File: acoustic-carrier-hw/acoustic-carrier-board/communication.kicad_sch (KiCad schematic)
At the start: 46 parts, among them IC1 ECP5-BGA256, J9 HR911130A, U1 KSZ9031RN, Y1 25MHz

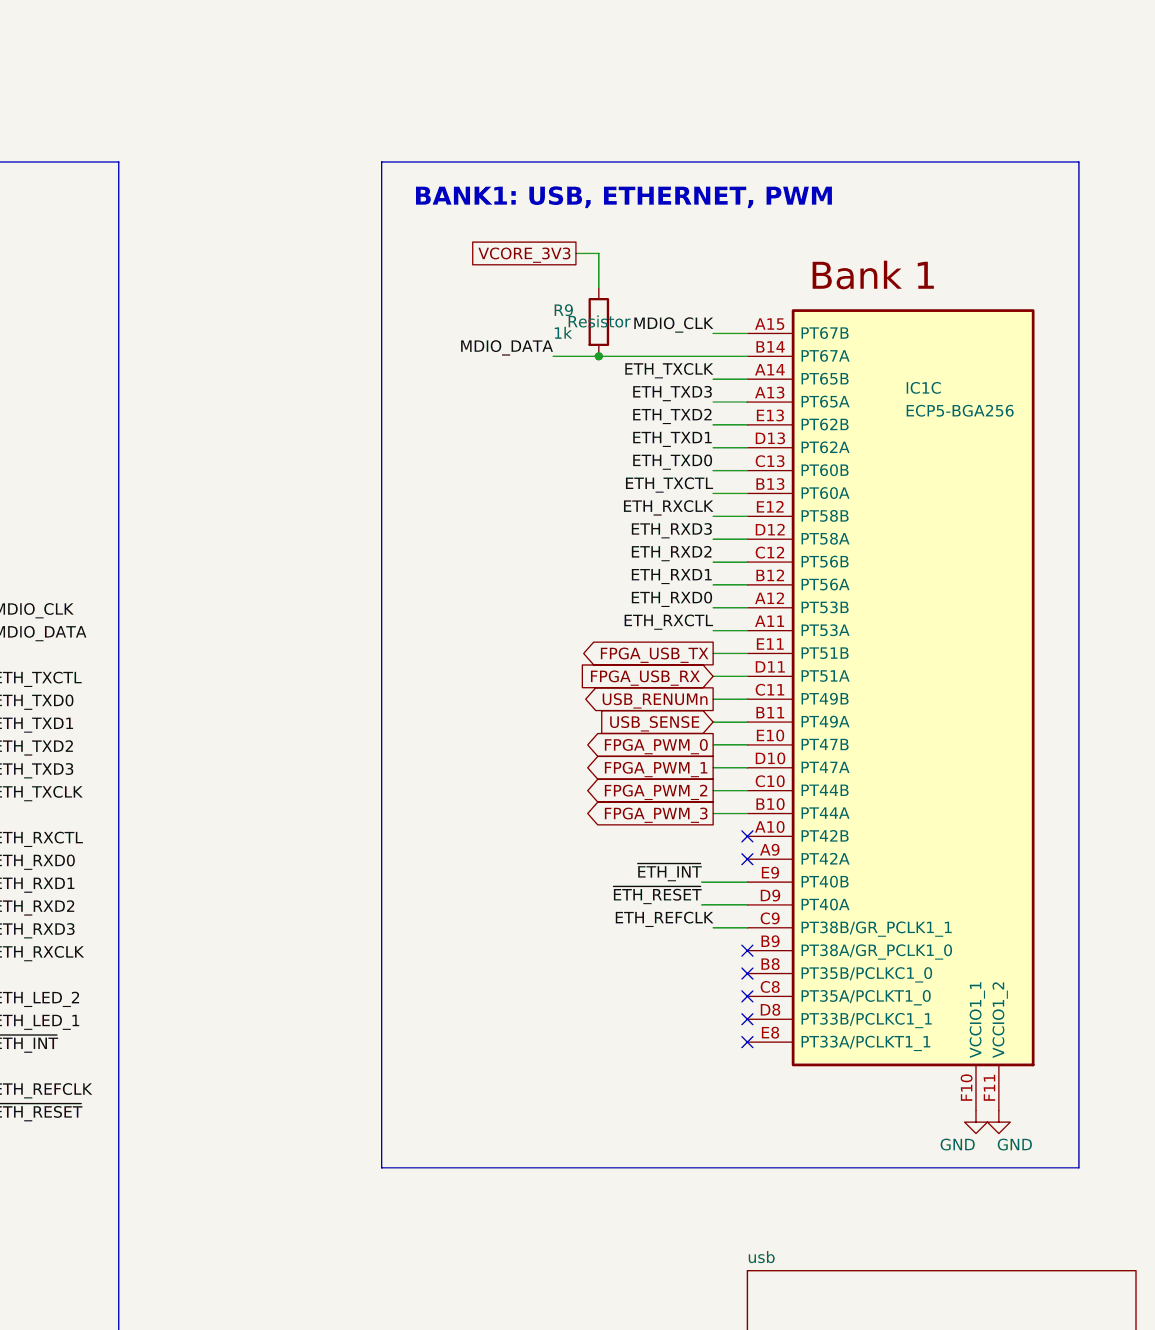
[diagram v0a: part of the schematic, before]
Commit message: [carrier] Fixed minor symbol errors, added minor routing info (next) continue schematic check
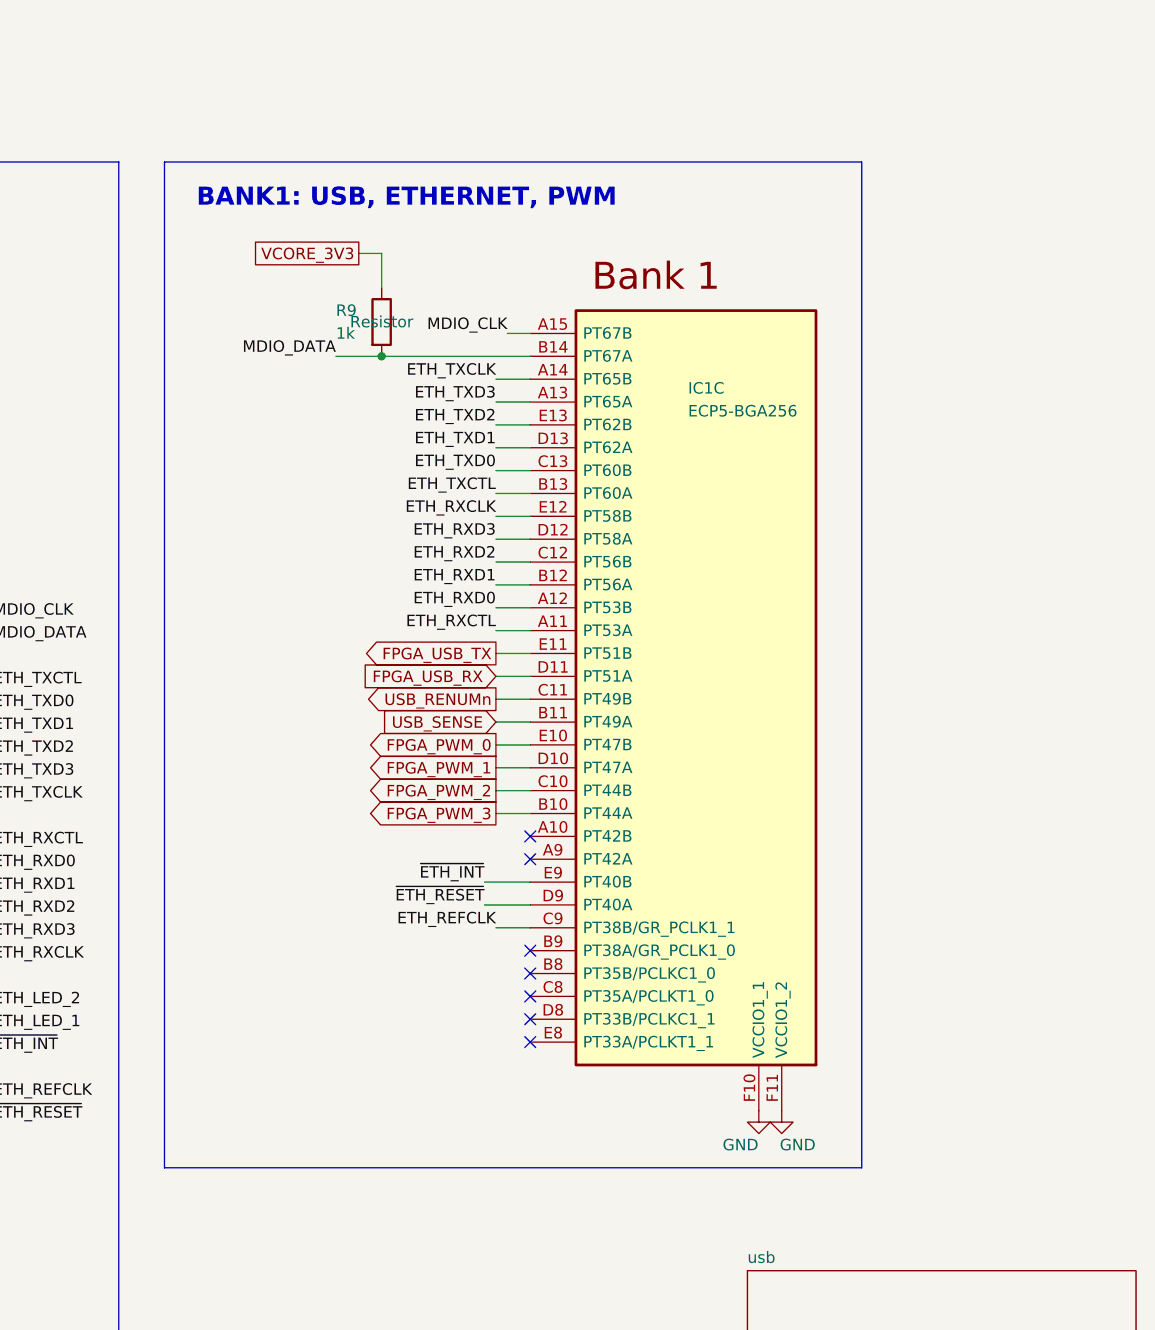
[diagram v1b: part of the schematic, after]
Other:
- moved on the sheet: IC1C, R9

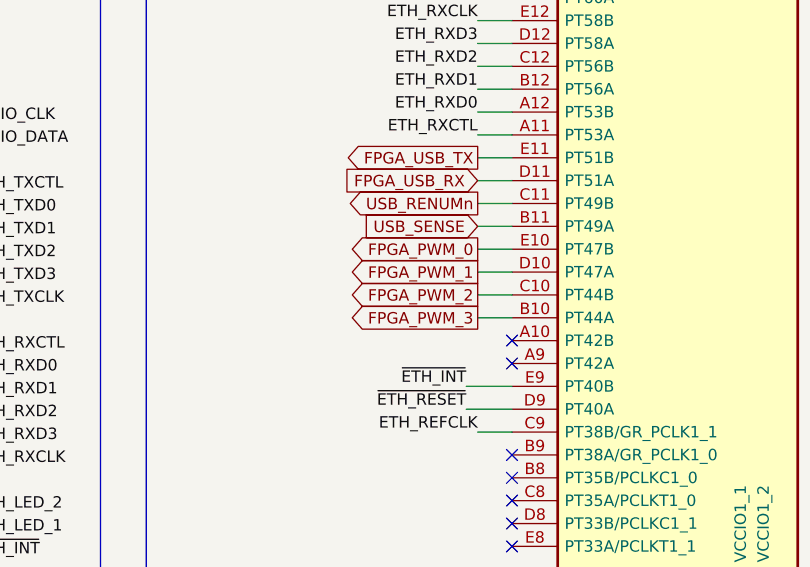
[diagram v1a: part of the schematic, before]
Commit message: [carrier] Review of adc_connections-page done
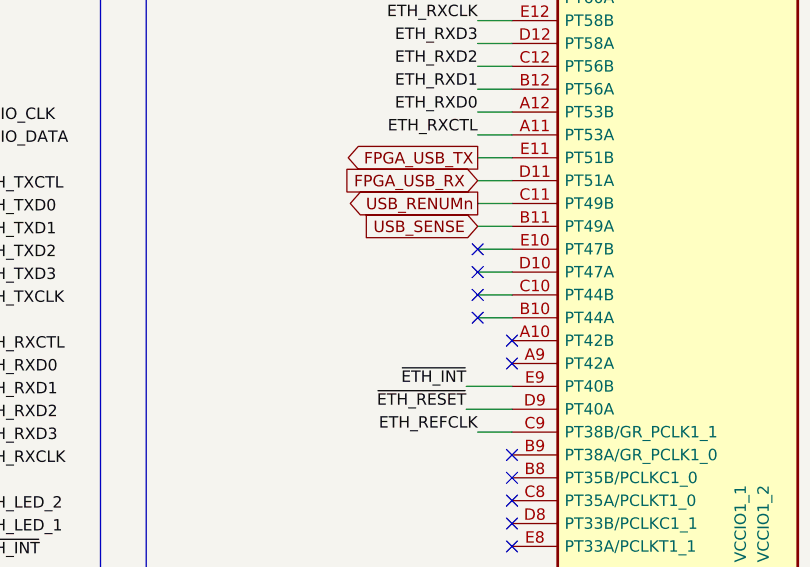
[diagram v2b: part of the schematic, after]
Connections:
- net FPGA_PWM_0: no longer names the net of IC1.E10 (PT47B)
- net FPGA_PWM_1: no longer names the net of IC1.D10 (PT47A)
- net FPGA_PWM_2: no longer names the net of IC1.C10 (PT44B)
- net FPGA_PWM_3: no longer names the net of IC1.B10 (PT44A)
- no-connect marks 8 -> 12
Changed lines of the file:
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@@
+	)
+	(no_connect
+		(at 207.01 85.09)
 	)
 	(no_connect
@@
 		(at 210.82 113.03)
 	)
+	(no_connect
+		(at 207.01 82.55)
+	)
+	(no_connect
+		(at 207.01 87.63)
+	)
+	(no_connect
+		(at 207.01 80.01)
+	)
 	(wire
 		(pts
@@
 			)
 			(justify left bottom)
-		)
-	)
-	(global_label "FPGA_PWM_1"
-		(shape output)
-		(at 207.01 82.55 180)
-		(fields_autoplaced yes)
-		(effects
-			(font
-				(size 1.27 1.27)
-			)
-			(justify right)
-		)
-		(property "Intersheetrefs" "${INTERSHEET_REFS}"
-			(at 191.9901 82.55 0)
-			(effects
-				(font
-					(size 1.27 1.27)
-				)
-				(justify right)
-				(hide yes)
-			)
 		)
 	)
@@
 		)
 	)
-	(global_label "FPGA_PWM_0"
-		(shape output)
-		(at 207.01 80.01 180)
-		(fields_autoplaced yes)
-		(effects
-			(font
-				(size 1.27 1.27)
-			)
-			(justify right)
-		)
-		(property "Intersheetrefs" "${INTERSHEET_REFS}"
-			(at 191.9901 80.01 0)
-			(effects
-				(font
-					(size 1.27 1.27)
-				)
-				(justify right)
-				(hide yes)
-			)
-		)
-	)
 	(global_label "VCORE_3V3"
 		(shape passive)
@@
 		)
 	)
-	(global_label "FPGA_PWM_2"
-		(shape output)
-		(at 207.01 85.09 180)
-		(fields_autoplaced yes)
-		(effects
-			(font
-				(size 1.27 1.27)
-			)
-			(justify right)
-		)
-		(property "Intersheetrefs" "${INTERSHEET_REFS}"
-			(at 191.9901 85.09 0)
-			(effects
-				(font
-					(size 1.27 1.27)
-				)
-				(justify right)
-				(hide yes)
-			)
-		)
-	)
 	(global_label "VCORE_3V3"
 		(shape passive)
@@
 			(effects
 				(font
-					(size 1.27 1.27)
-				)
-				(justify right)
-				(hide yes)
-			)
-		)
-	)
-	(global_label "FPGA_PWM_3"
-		(shape output)
-		(at 207.01 87.63 180)
-		(fields_autoplaced yes)
-		(effects
-			(font
-				(size 1.27 1.27)
-			)
-			(justify right)
-		)
-		(property "Intersheetrefs" "${INTERSHEET_REFS}"
-			(at 191.9901 87.63 0)
-			(effects
-				(font

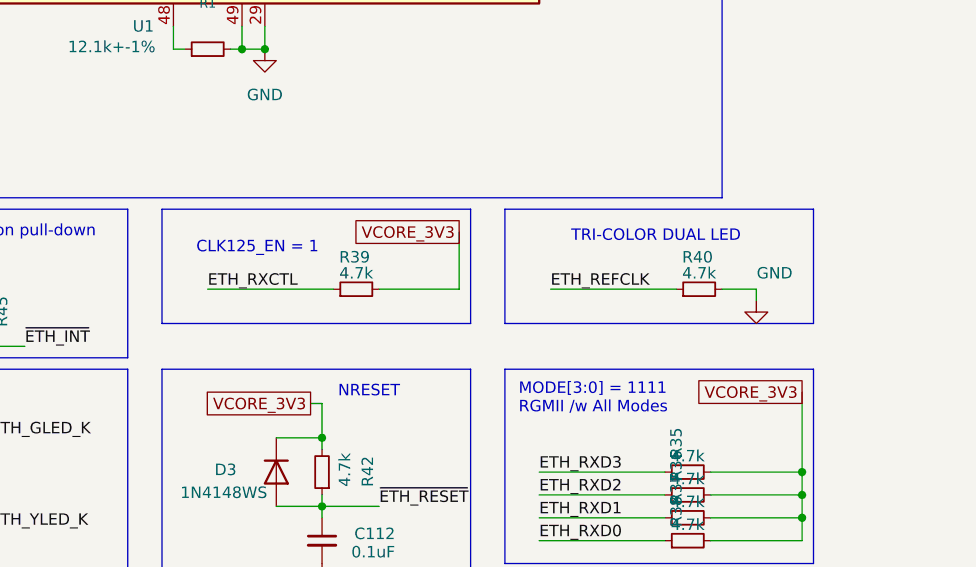
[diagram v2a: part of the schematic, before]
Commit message: [carrier] Finished flash and config check
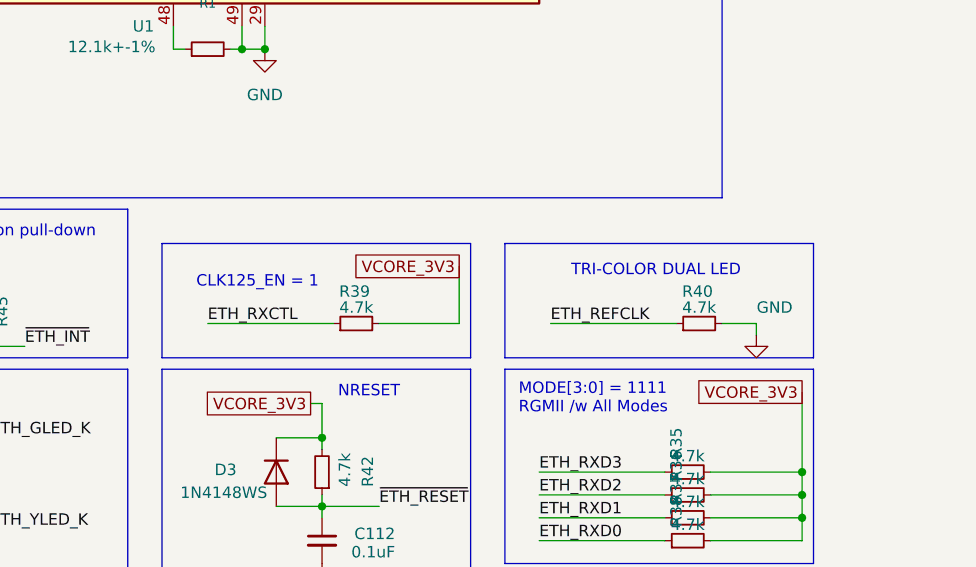
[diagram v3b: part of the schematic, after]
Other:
- moved on the sheet: R39, R40
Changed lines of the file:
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@@
 	(paper "A4")
 	(rectangle
-		(start 140.97 152.4)
-		(end 175.26 165.1)
+		(start 140.97 156.21)
+		(end 175.26 168.91)
 		(stroke
 			(width 0)
@@
 	)
 	(rectangle
-		(start 102.87 152.4)
-		(end 137.16 165.1)
+		(start 102.87 156.21)
+		(end 137.16 168.91)
 		(stroke
 			(width 0)
@@
 	(text "TRI-COLOR DUAL LED"
 		(exclude_from_sim no)
-		(at 148.336 156.21 0)
+		(at 148.336 160.02 0)
 		(effects
 			(font
@@
 	(text "CLK125_EN = 1"
 		(exclude_from_sim no)
-		(at 106.68 157.48 0)
+		(at 106.68 161.29 0)
 		(effects
 			(font
@@
 	(wire
 		(pts
-			(xy 127 161.29) (xy 135.89 161.29)
+			(xy 127 165.1) (xy 135.89 165.1)
 		)
 		(stroke
@@
 	(wire
 		(pts
-			(xy 165.1 161.29) (xy 168.91 161.29)
+			(xy 165.1 165.1) (xy 168.91 165.1)
 		)
 		(stroke
@@
 	(wire
 		(pts
-			(xy 107.95 161.29) (xy 121.92 161.29)
+			(xy 107.95 165.1) (xy 121.92 165.1)
 		)
 		(stroke
@@
 	(wire
 		(pts
-			(xy 135.89 154.94) (xy 135.89 161.29)
+			(xy 135.89 158.75) (xy 135.89 165.1)
 		)
 		(stroke
@@
 	(wire
 		(pts
-			(xy 146.05 161.29) (xy 160.02 161.29)
+			(xy 146.05 165.1) (xy 160.02 165.1)
 		)
 		(stroke
@@
 	(wire
 		(pts
-			(xy 168.91 161.29) (xy 168.91 162.56)
+			(xy 168.91 165.1) (xy 168.91 166.37)
 		)
 		(stroke
@@
 	)
 	(label "ETH_REFCLK"
-		(at 146.05 161.29 0)
+		(at 146.05 165.1 0)
 		(effects
 			(font
@@
 	)
 	(label "ETH_RXCTL"
-		(at 107.95 161.29 0)
+		(at 107.95 165.1 0)
 		(effects
 			(font
@@
 	(global_label "VCORE_3V3"
 		(shape passive)
-		(at 135.89 154.94 180)
+		(at 135.89 158.75 180)
 		(fields_autoplaced yes)
 		(effects
@@
 		)
 		(property "Intersheetrefs" "${INTERSHEET_REFS}"
-			(at 123.4328 154.94 0)
+			(at 123.4328 158.75 0)
 			(effects
 				(font
@@
 	(symbol
 		(lib_id "power:GND")
-		(at 168.91 162.56 0)
+		(at 168.91 166.37 0)
 		(unit 1)
 		(exclude_from_sim no)
@@
 		(dnp no)
 		(property "Reference" "#PWR075"
-			(at 168.91 168.91 0)
+			(at 168.91 172.72 0)
 			(effects
 				(font
@@
 		)
 		(property "Value" "GND"
-			(at 170.942 159.512 0)
+			(at 170.942 163.322 0)
 			(effects
 				(font
@@
 		)
 		(property "Footprint" ""
-			(at 168.91 162.56 0)
+			(at 168.91 166.37 0)
 			(effects
 				(font
@@
 		)
 		(property "Datasheet" ""
-			(at 168.91 162.56 0)
+			(at 168.91 166.37 0)
 			(effects
 				(font
@@
 		)
 		(property "Description" "Power symbol creates a global label with name \"GND\" , ground"
-			(at 168.91 162.56 0)
+			(at 168.91 166.37 0)
 			(effects
 				(font
@@
 	(symbol
 		(lib_id "Device:R_Small")
-		(at 162.56 161.29 90)
+		(at 162.56 165.1 90)
 		(unit 1)
 		(exclude_from_sim no)
@@
 		(dnp no)
 		(property "Reference" "R40"
-			(at 164.084 157.734 90)
+			(at 164.084 161.544 90)
 			(effects
 				(font
@@
 		)
 		(property "Value" "4.7k"
-			(at 162.56 159.512 90)
+			(at 162.56 163.322 90)
 			(effects
 				(font
@@
 		)
 		(property "Footprint" "Resistor_SMD:R_0402_1005Metric"
-			(at 162.56 161.29 0)
+			(at 162.56 165.1 0)
 			(effects
 				(font
@@
 		)
 		(property "Datasheet" "~"
-			(at 162.56 161.29 0)
+			(at 162.56 165.1 0)
 			(effects
 				(font
@@
 		)
 		(property "Description" "Resistor, small symbol"
-			(at 162.56 161.29 0)
+			(at 162.56 165.1 0)
 			(effects
 				(font
@@
 		)
 		(property "LCSC Part Number" ""
-			(at 162.56 161.29 0)
+			(at 162.56 165.1 0)
 			(effects
 				(font
@@
 		)
 		(property "Manufacturing Part Number" ""
-			(at 162.56 161.29 0)
+			(at 162.56 165.1 0)
 			(effects
 				(font
@@
 		)
 		(property "LPN" "0402WGF4701TCE"
-			(at 162.56 161.29 90)
+			(at 162.56 165.1 90)
 			(effects
 				(font
@@
 		)
 		(property "MPN" "C25900"
-			(at 162.56 161.29 90)
+			(at 162.56 165.1 90)
 			(effects
 				(font
@@
 		)
 		(property "Part Number" ""
-			(at 162.56 161.29 90)
+			(at 162.56 165.1 90)
 			(effects
 				(font
@@
 		)
 		(property "SN-DK" ""
-			(at 162.56 161.29 90)
+			(at 162.56 165.1 90)
 			(effects
 				(font
@@
 		)
 		(property "Sim.Pin" ""
-			(at 162.56 161.29 90)
+			(at 162.56 165.1 90)
 			(effects
 				(font
@@
 		)
 		(property "LCSC Part" ""
-			(at 162.56 161.29 90)
+			(at 162.56 165.1 90)
 			(effects
 				(font
@@
 	(symbol
 		(lib_id "Device:R_Small")
-		(at 124.46 161.29 90)
+		(at 124.46 165.1 90)
 		(unit 1)
 		(exclude_from_sim no)
@@
 		(dnp no)
 		(property "Reference" "R39"
-			(at 125.984 157.734 90)
+			(at 125.984 161.544 90)
 			(effects
 				(font
@@
 		)
 		(property "Value" "4.7k"
-			(at 124.46 159.512 90)
+			(at 124.46 163.322 90)
 			(effects
 				(font
@@
 		)
 		(property "Footprint" "Resistor_SMD:R_0402_1005Metric"
-			(at 124.46 161.29 0)
+			(at 124.46 165.1 0)
 			(effects
 				(font
@@
 		)
 		(property "Datasheet" "~"
-			(at 124.46 161.29 0)
+			(at 124.46 165.1 0)
 			(effects
 				(font
@@
 		)
 		(property "Description" "Resistor, small symbol"
-			(at 124.46 161.29 0)
+			(at 124.46 165.1 0)
 			(effects
 				(font
@@
 		)
 		(property "LCSC Part Number" ""
-			(at 124.46 161.29 0)
+			(at 124.46 165.1 0)
 			(effects
 				(font
@@
 		)
 		(property "Manufacturing Part Number" ""
-			(at 124.46 161.29 0)
+			(at 124.46 165.1 0)
 			(effects
 				(font
@@
 		)
 		(property "LPN" "0402WGF4701TCE"
-			(at 124.46 161.29 90)
+			(at 124.46 165.1 90)
 			(effects
 				(font
@@
 		)
 		(property "MPN" "C25900"
-			(at 124.46 161.29 90)
+			(at 124.46 165.1 90)
 			(effects
 				(font
@@
 		)
 		(property "Part Number" ""
-			(at 124.46 161.29 90)
+			(at 124.46 165.1 90)
 			(effects
 				(font
@@
 		)
 		(property "SN-DK" ""
-			(at 124.46 161.29 90)
+			(at 124.46 165.1 90)
 			(effects
 				(font
@@
 		)
 		(property "Sim.Pin" ""
-			(at 124.46 161.29 90)
+			(at 124.46 165.1 90)
 			(effects
 				(font
@@
 		)
 		(property "LCSC Part" ""
-			(at 124.46 161.29 90)
+			(at 124.46 165.1 90)
 			(effects
 				(font
